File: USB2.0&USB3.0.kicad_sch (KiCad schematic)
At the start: 22 parts, among them U5 ULC0524P

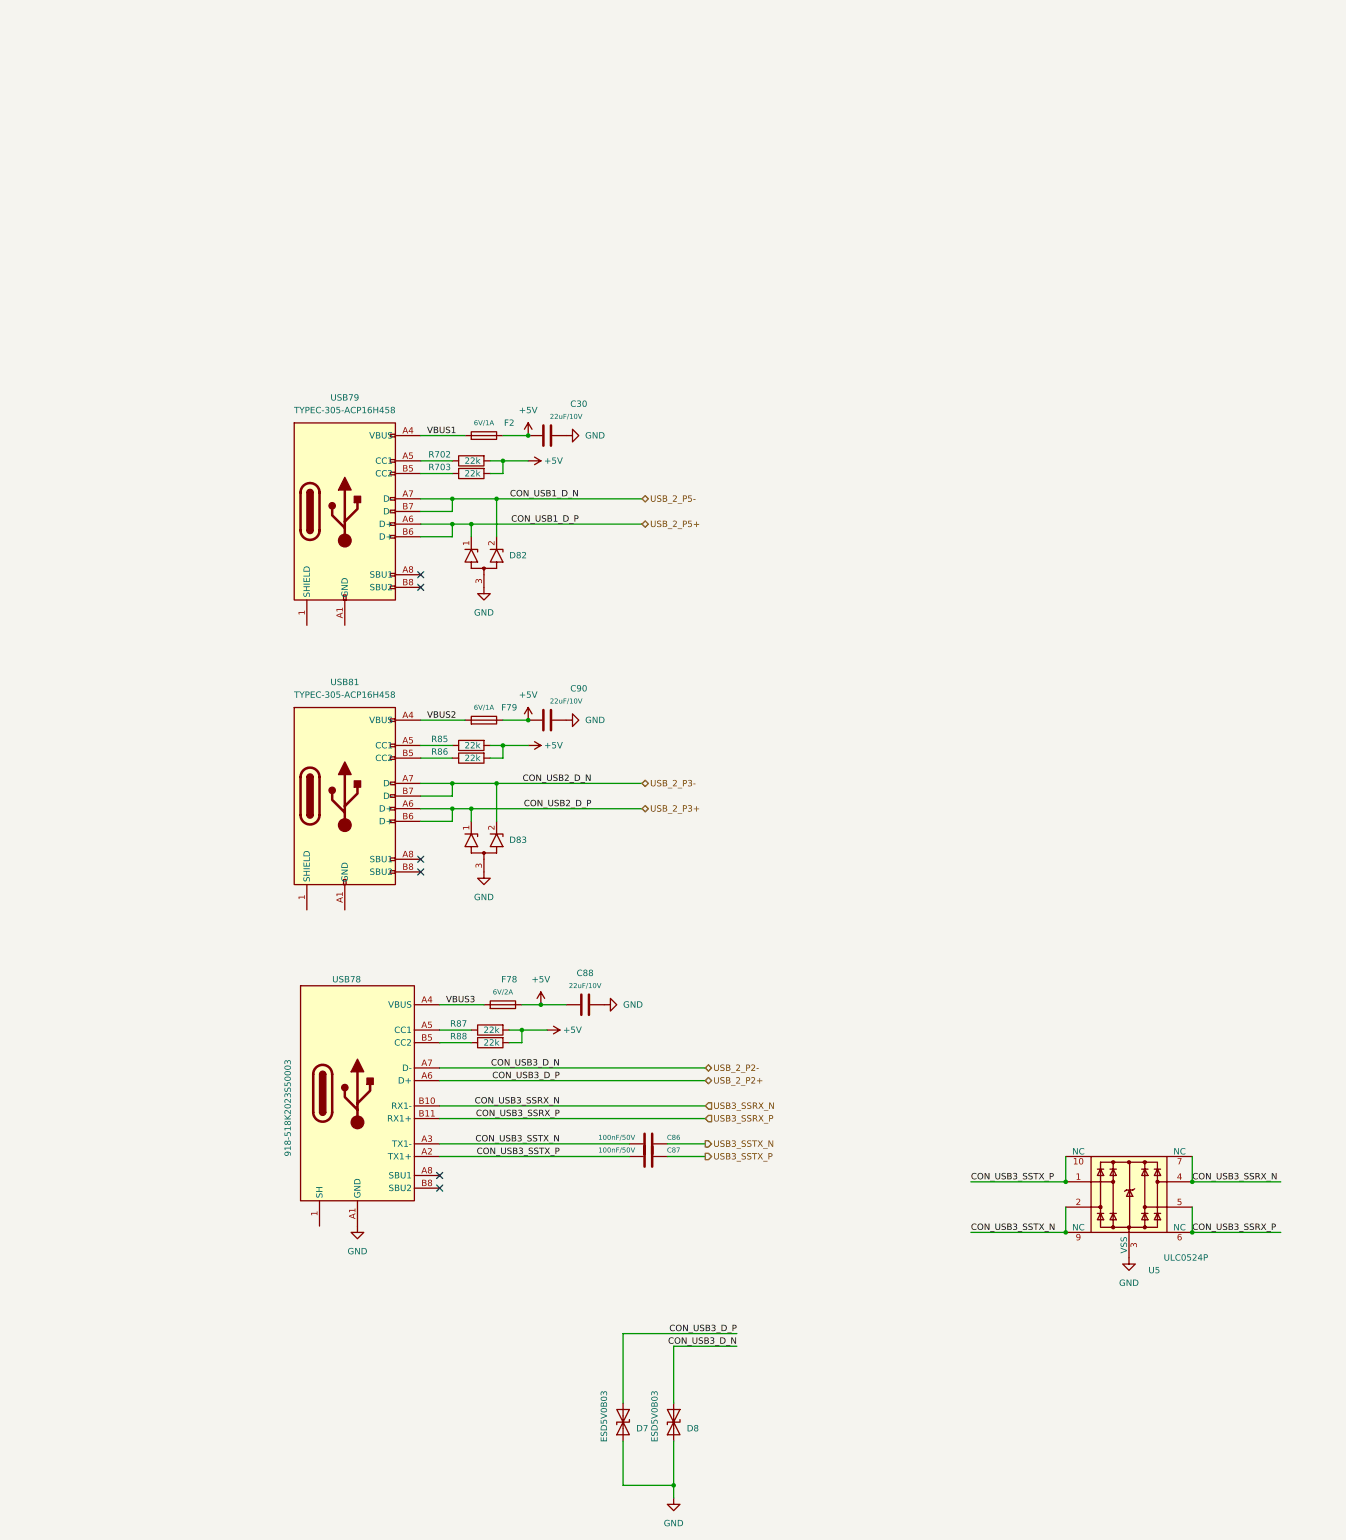
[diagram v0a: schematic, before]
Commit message: hierarchical schema rework
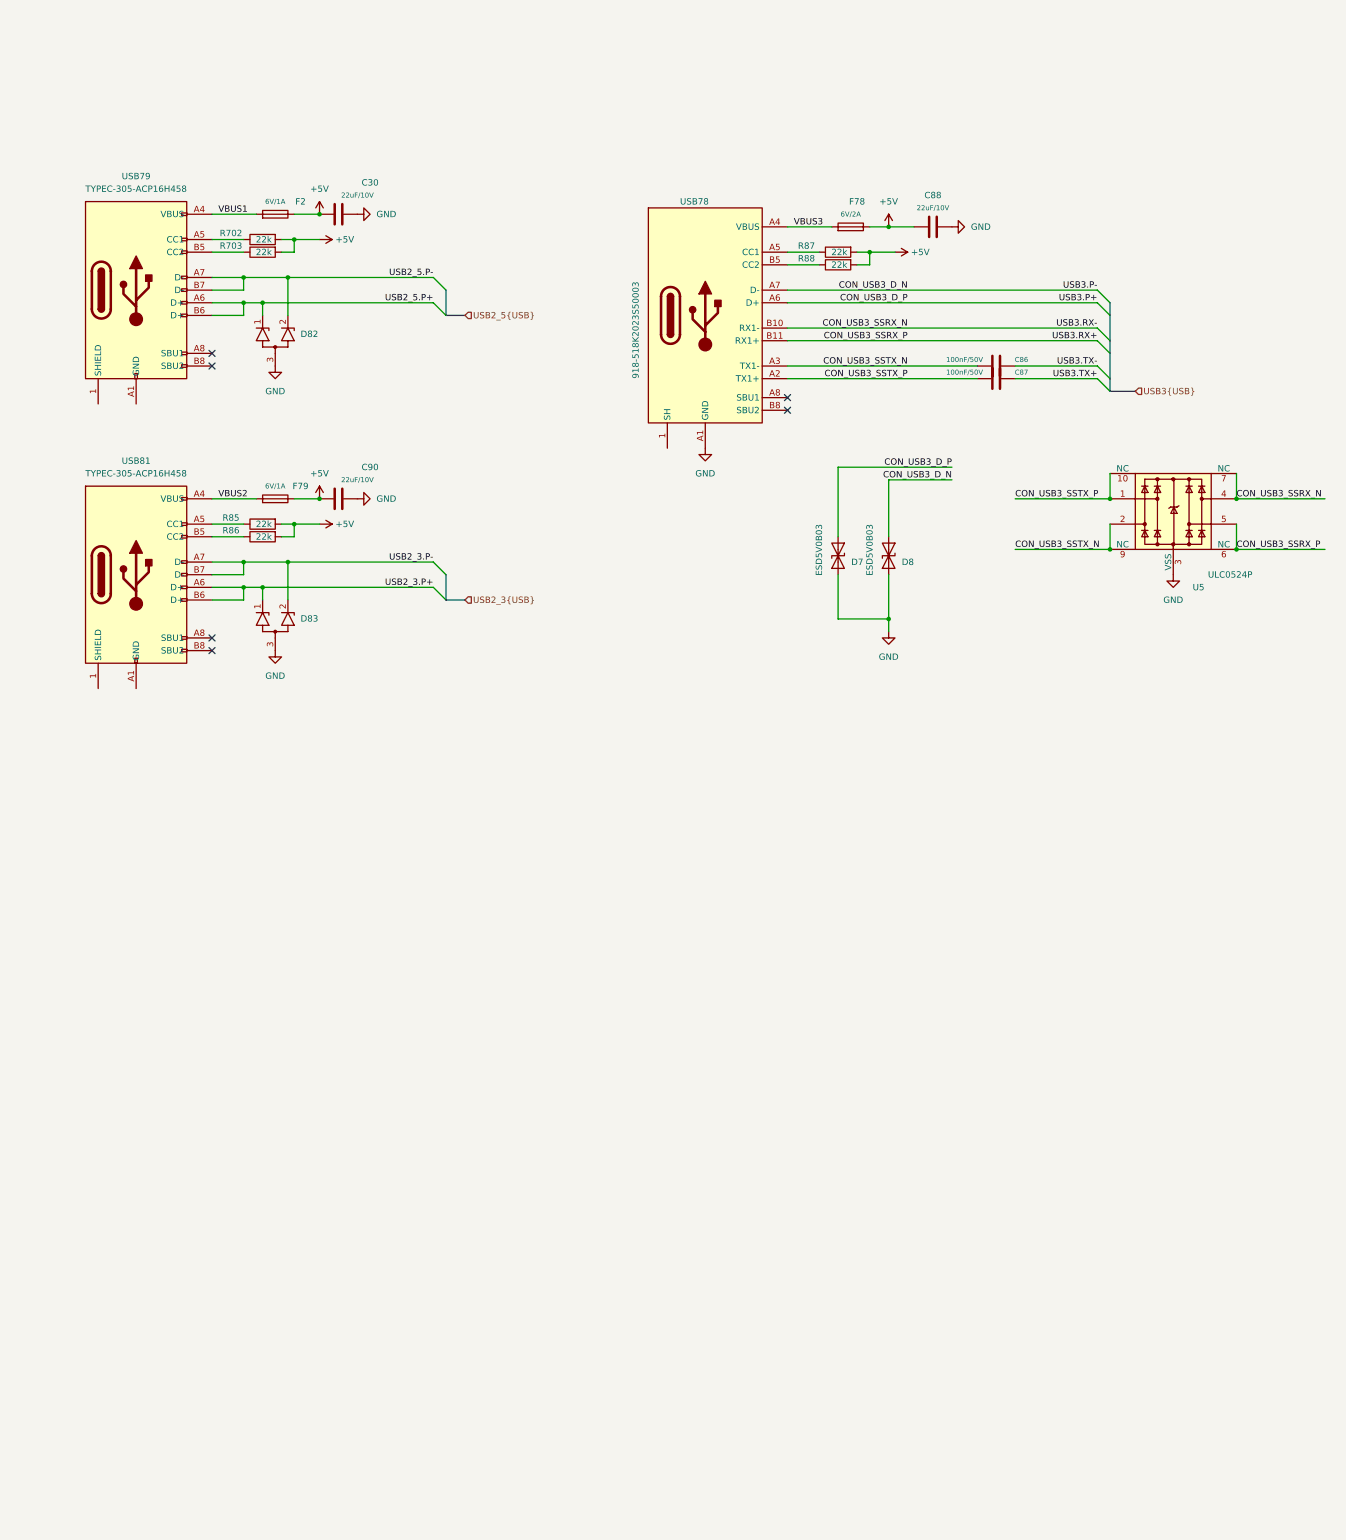
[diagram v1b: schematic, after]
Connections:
- net USB3_SSRX_N renamed CON_USB3_SSRX_N
- net USB3_SSRX_P renamed CON_USB3_SSRX_P
- net USB3_SSTX_N renamed USB3.TX-
- net USB3_SSTX_P renamed USB3.TX+
- net USB_2_P2+ renamed CON_USB3_D_P
- net USB_2_P2- renamed CON_USB3_D_N
- net USB_2_P3+ renamed USB2_3.P+
- net USB_2_P3- renamed USB2_3.P-
- net USB_2_P5+ renamed USB2_5.P+
- net USB_2_P5- renamed USB2_5.P-
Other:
- moved on the sheet: C30, C86, C87, C88, C90, D7, D8, D82, D83, F2, F78, F79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

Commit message: prod files created
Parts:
- added C148, C149, C150: 100nF/50V, Capacitor_SMD:C_0402_1005Metric, symbol Device:C_Small
- added R154, R155, R156: 1M/1%, A_HDJ_Library:R_0402_1005Metric, symbol Device:R_Small
- renumbered C30 to C88, C88 to C89, C86 to C90, C87 to C91, C90 to C92, D7 to D83, D8 to D84, D83 to D85, F2 to F79, F78 to F80, F79 to F81, R702 to R101, R703 to R102, R87 to R103, R88 to R104, R85 to R105, R86 to R106, U5 to U80, USB79 to USB78, USB78 to USB79, USB81 to USB80
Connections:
- net GND: now also USB78.A1 (GND), USB78.A12 (GND), USB78.B1 (GND), USB78.B12 (GND), USB80.A1 (GND), USB80.A12 (GND), USB80.B1 (GND), USB80.B12 (GND), C148.2, C149.2, C150.2, R154.2, R155.2, R156.2
- net at USB79.1 (SH), USB79.2 (SH), USB79.3 (SH)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: now also C150.1, R156.1
- net at USB78.1 (SHIELD): now also C149.1, R155.1
- net at USB80.1 (SHIELD): now also C148.1, R154.1
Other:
- note added: "[USB]"
- moved on the sheet: C92, D85, F81, R105, R106, USB80
